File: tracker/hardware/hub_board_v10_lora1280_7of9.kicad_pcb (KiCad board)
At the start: 4 copper layers, 72 x 80 mm, 49 parts, among them U1 U1, U2 U2, U3 U3, U5 U5, U6 U6, U7 U7

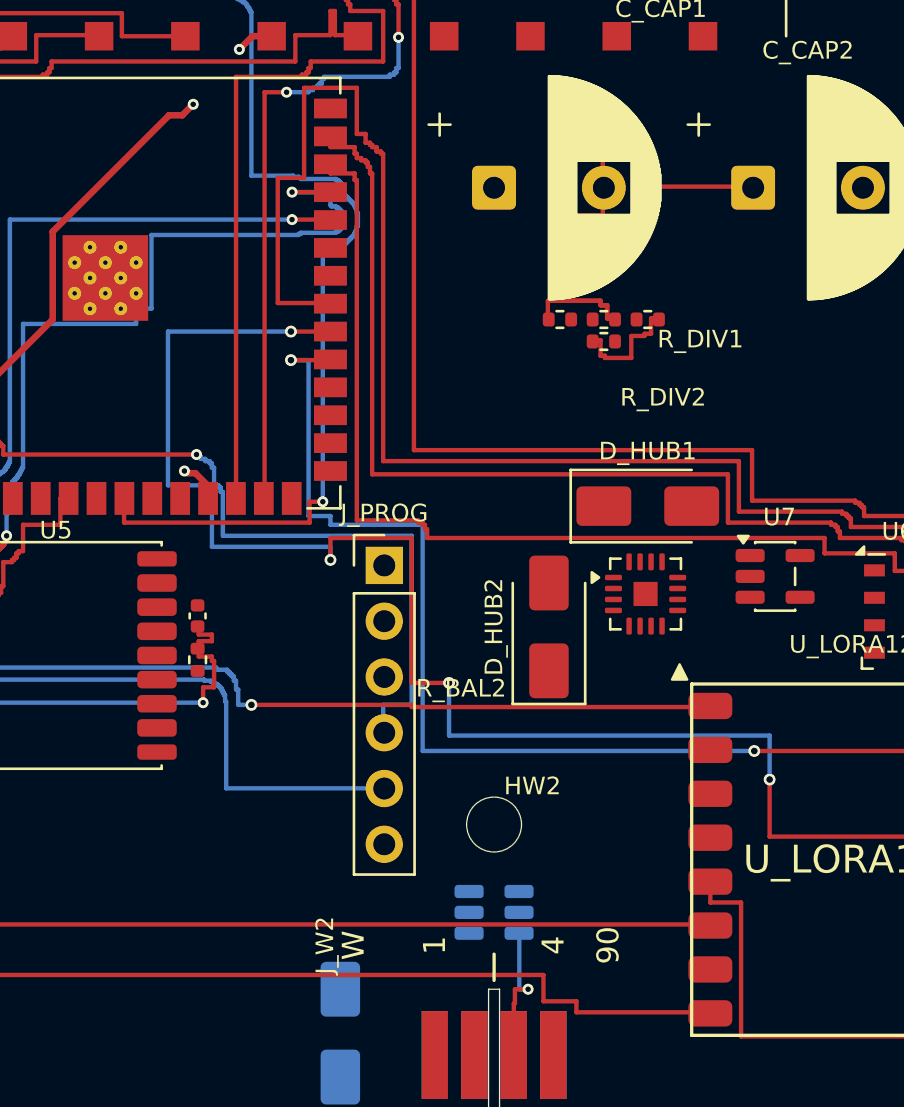
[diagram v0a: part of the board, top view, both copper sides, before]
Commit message: consolidation: pr/lora1280-interactive-merged -> master (#375)
* feat(hub): operator's hand-routing of SPI1_SCK and E28_DIO3, folded onto current master

Operator routed both remaining LoRa1280 interface nets by hand in KiCad on the T14, moving several
existing lanes to open the corridors. That work is preserved verbatim here (commit c51c1e45 on
c03rad0r/balloon-fresh-1) with two things added because his base predated them:

  1. F33_VCC and F33_RESET_N re-routed on top, so merging this does not silently delete the two
     nets that landed in bd96d565 after he branched.
  2. Zones refilled. His saved board carried a STALE pour, which read as 136 violations with 46
     clearance. After the refill: 79 violations, 5 clearance. Those 46 were not routing errors --
     they were the old GND pour still sitting where his new tracks now run.

STATE OF THIS BRANCH -- deliberately NOT clean enough to merge:
  LoRa1280 interface   9/9 routed (no unconnected item names SPI1_SCK or E28_DIO3)
  violations           79
  clearance             5   <- REAL, see below
  shorting_items        0
  solder_mask_bridge    0

The five clearance violations, all between 0.149 and 0.161 mm against a 0.200 mm rule:
  * Track /E28_RESET_N (B.Cu) vs segment /SPI1_SCK (B.Cu)  -- 0.1487 mm, twice
  * Segment /SPI1_SCK (F.Cu) vs Pad 21 /F33_VSENSE of U1   -- 0.1533 mm
  * Segment /I2C_SDA (F.Cu) vs segment /I2C_SCL (F.Cu)     -- 0.1606 mm, twice
Each needs about 0.05 mm of breathing room. They are NOT relaxed away: the board rule stays 0.20.
Hand-routes cannot be nudged by the maze router without destroying the operator's work, so these go
back to him with the exact locations.

Also present: Pad 14 [GND] of U_LORA1280 reports "missing connection" to zone GND_FCu. Introduced by
the refill on this board, not by his routing; it is a thermal-spoke question for the next pass.

.gitignore now covers fp-info-cache, *.lck and ~*.kicad_pcb.lck -- KiCad writes both constantly and
they were showing up in th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
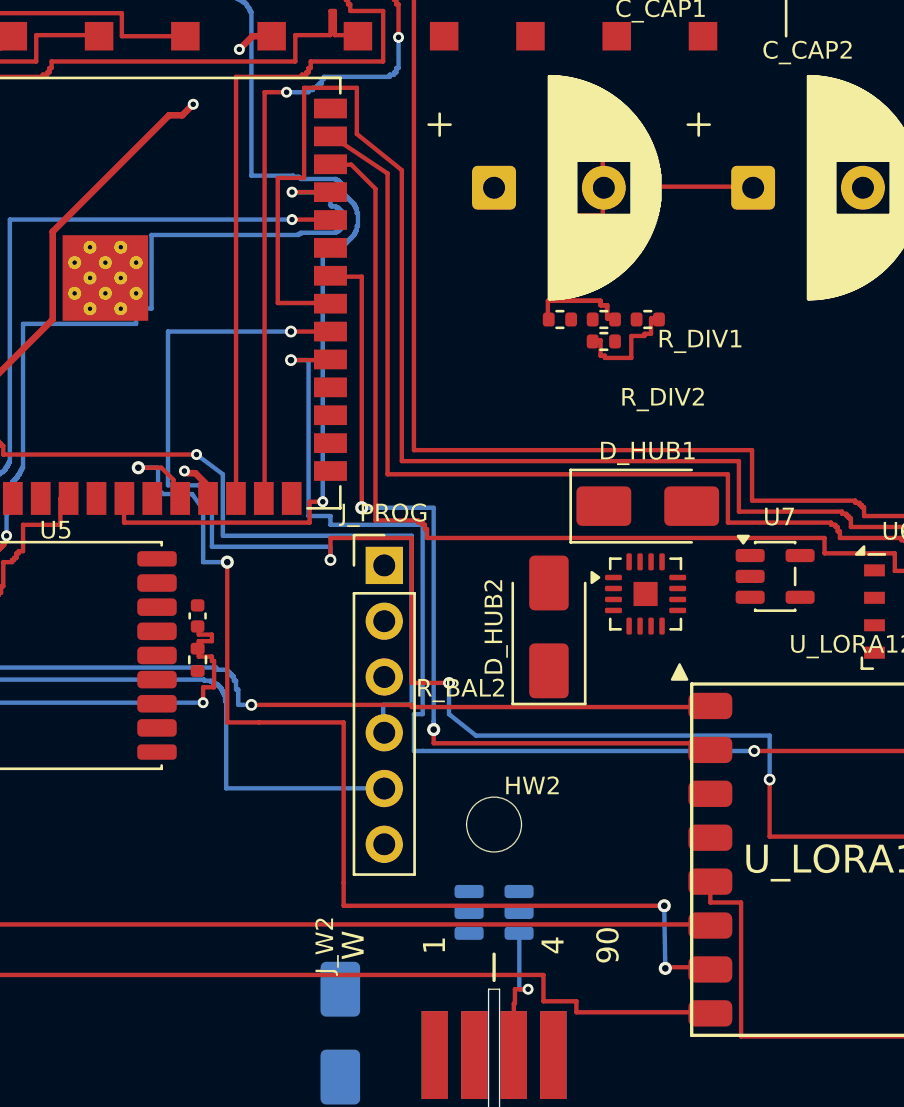
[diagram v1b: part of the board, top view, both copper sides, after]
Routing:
- net /SPI1_SCK: track 0.00 -> 50.9 mm, vias 0 -> 4
- net /E28_DIO3: track 0.00 -> 37.9 mm, vias 0 -> 2
- net /USB_DN: track 36.1 -> 33.4 mm
- net /I2C_SDA: track 49.7 -> 48.5 mm
- net /E28_DIO1: track 74.4 -> 73.3 mm
- net /E28_RESET_N: track 71.4 -> 70.4 mm
- net /E28_BUSY: track 53.0 -> 53.8 mm
- net /I2C_SCL: track 45.4 -> 44.7 mm
